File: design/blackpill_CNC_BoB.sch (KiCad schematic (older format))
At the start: 297 parts, among them J101 ALimIN, J102 ZLimIN, J103 YLimIN, J104 XLimIN, J105 CS_IN, J106 FH_IN, J107 DoorIN, J108 ResetIN, J109 ProbeIN, J110 12V Power in, J111 AuxEncIn, J112 5V Power out, J113 ADC_in_1, J114 ADC_in_2, J115 stepDriverLim, J116 Reset, J117 UART1, J118 I2C, J119 SpindleVFD, J120 Spindle/Coolant, J121 Spindle, J122 Coolant, J123 AuxOut, J124 XStepDrv, J125 YStepDrv, J126 ZStepDrv, J127 AStepDrv, U101 TLP290-4, U102 TLP290-4, U103 TLP290-4, U104 74LVC2G17, U105 LD1117S50TR_SOT223, U106 LM358, U107 TLV9001, U108 TLV9001, U109 YAAJ_WeAct_BlackPill_Part_Like, U110 TLV9001, U111 TLV9001, U112 74HCT541, U113 74HCT541, U114 74HCT541, U115 ULN2003A, U116 ULN2003A, U117 ULN2003A

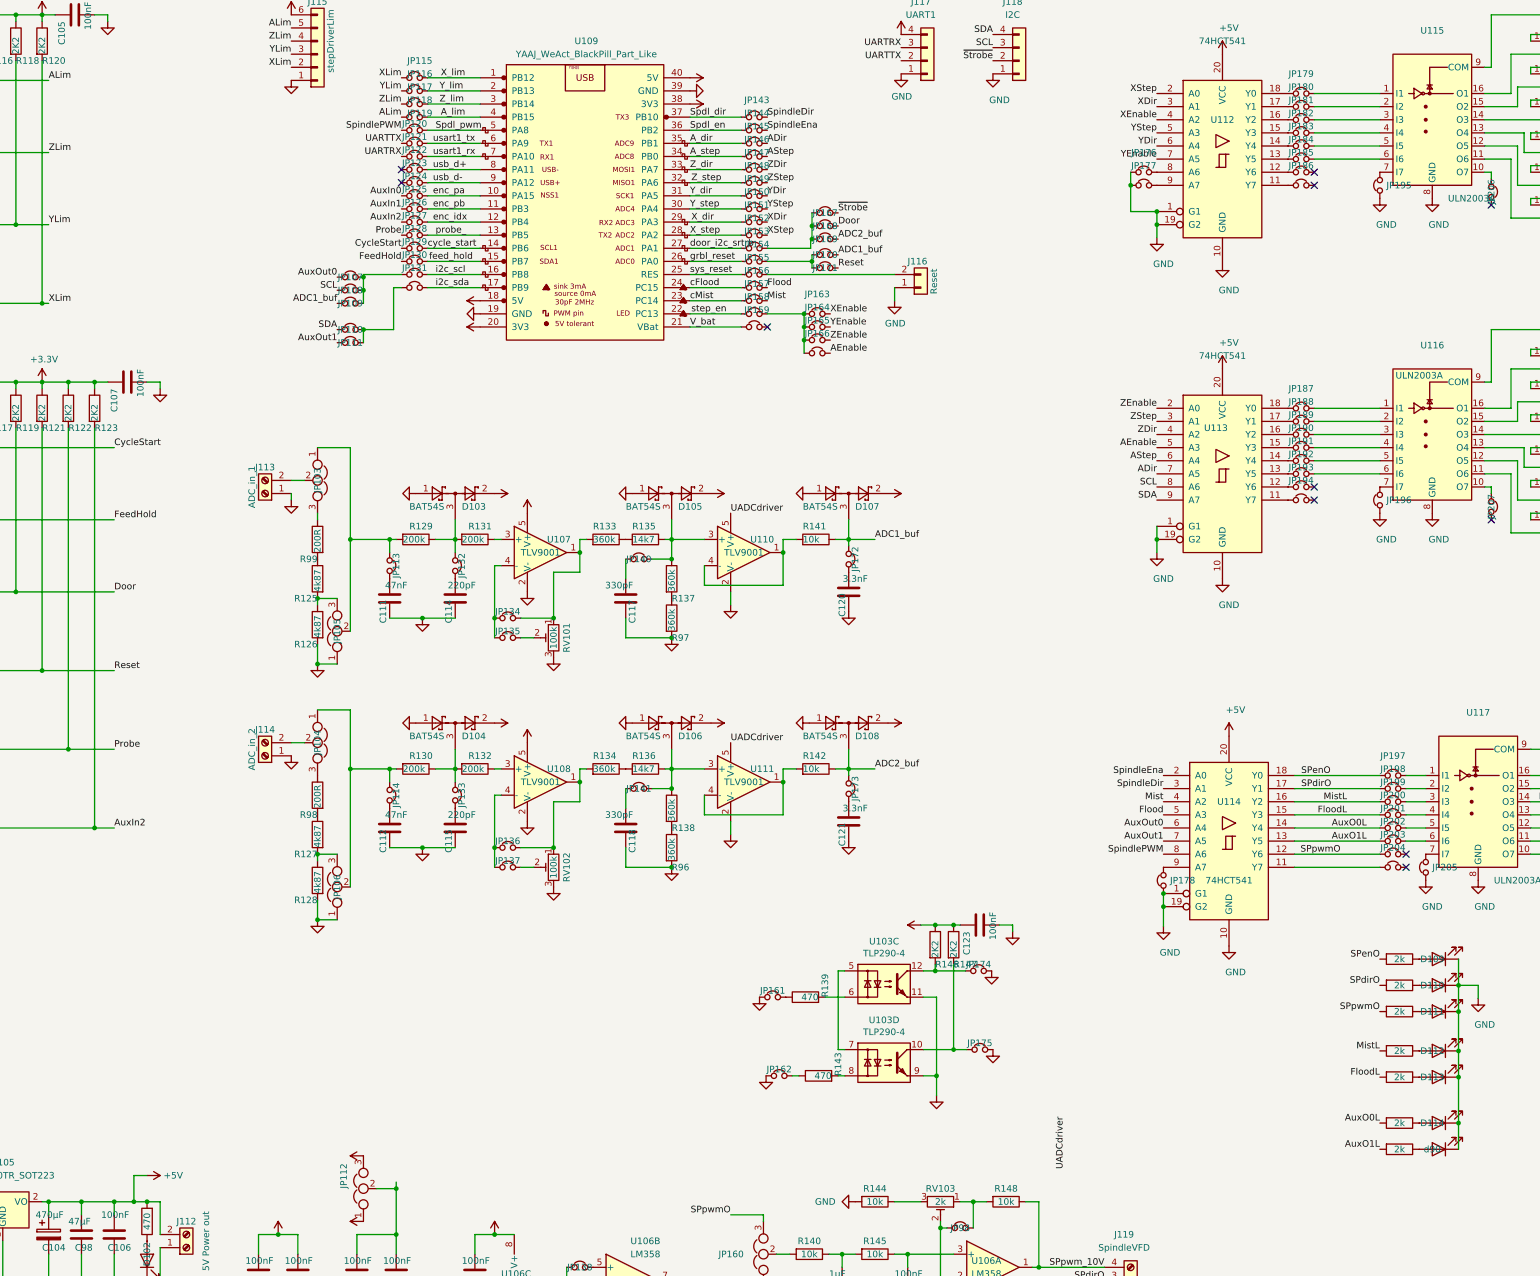
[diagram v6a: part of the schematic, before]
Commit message: add schottky to blackpill 5V
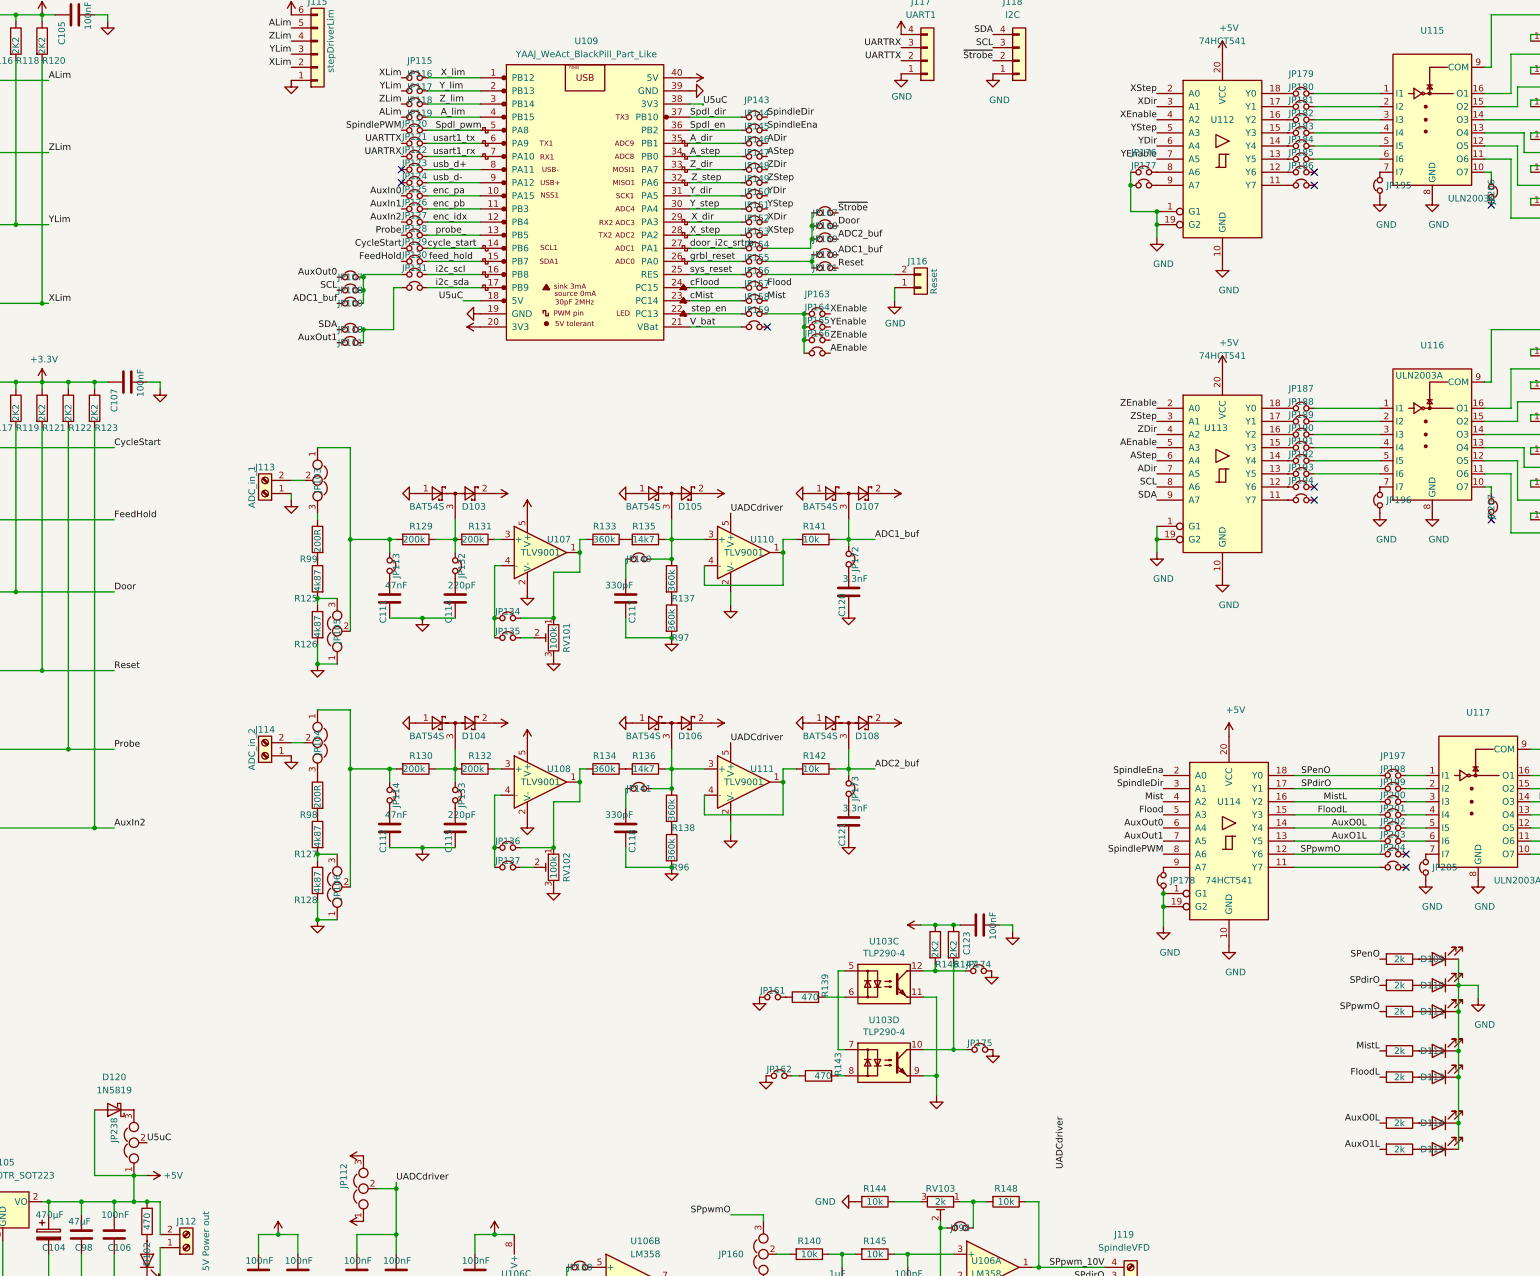
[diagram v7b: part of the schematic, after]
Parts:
- added D120: 1N5819, Diode_SMD:D_SOD-323, symbol Diode:1N5819
- added JP238: Jumper_NC_Dual, Connector_PinHeader_2.54mm:PinHeader_1x03_P2.54mm_Vertical, symbol Device:Jumper_NC_Dual
- renumbered d90 to D115, r90 to R167
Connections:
- net +5V: now also D120.2 (A), JP238.1; no longer U109.18 (5V), U109.38 (3V3)
- net UADCdriver: now also C110.1, C113.1, JP112.2
- new net: D120.1 (K), JP238.3
- new net U5uC: JP238.2, U109.18 (5V), U109.38 (3V3)
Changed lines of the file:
@@
 $EndComp
 $Comp
-L power:+5V #PWR0132
-U 1 1 6843DDDB
-P 6240 2980
-F 0 "#PWR0132" H 6240 2830 50  0001 C CNN
-F 1 "+5V" V 6260 3150 50  0001 L CNN
-F 2 "" H 6240 2980 50  0001 C CNN
-F 3 "" H 6240 2980 50  0001 C CNN
-	1    6240 2980
-	0    -1   -1   0
-$EndComp
-$Comp
 L power:GND #PWR0133
 U 1 1 6843E09C
@@
 	0    1    1    0
 $EndComp
-$Comp
-L power:+5V #PWR0152
-U 1 1 6860CDFC
-P 7840 1480
-F 0 "#PWR0152" H 7840 1330 50  0001 C CNN
-F 1 "+5V" V 7830 1620 50  0001 L CNN
-F 2 "" H 7840 1480 50  0001 C CNN
-F 3 "" H 7840 1480 50  0001 C CNN
-	1    7840 1480
-	0    1    1    0
-$EndComp
 NoConn ~ 8430 3180
 $Comp
@@
 Connection ~ 7700 7300
 $Comp
-L Device:R r90
+L Device:R R167
 U 1 1 67BECA90
 P 13250 9450
-F 0 "r90" V 13000 9450 50  0001 C CNN
+F 0 "R167" V 13000 9450 50  0001 C CNN
 F 1 "2k" V 13250 9450 50  0000 C CNN
 F 2 "Resistor_SMD:R_0603_1608Metric" V 13180 9450 50  0001 C CNN
@@
 $EndComp
 $Comp
-L Device:LED d90
+L Device:LED D115
 U 1 1 67BED2C6
 P 13550 9450
-F 0 "d90" H 13600 9450 50  0000 C CNN
+F 0 "D115" H 13600 9450 50  0000 C CNN
 F 1 "LED" H 13500 9250 50  0001 C CNN
 F 2 "LED_SMD:LED_0603_1608Metric" H 13550 9450 50  0001 C CNN
@@
 Wire Wire Line
 	2900 10850 3050 10850
+Text Label 5600 9700 0    50   ~ 0
+UADCdriver
+$Comp
+L Diode:1N5819 D120
+U 1 1 681EDD27
+P 3450 9150
+F 0 "D120" H 3450 8900 50  0000 C CNN
+F 1 "1N5819" H 3450 9000 50  0000 C CNN
+F 2 "Diode_SMD:D_SOD-323" H 3450 8975 50  0001 C CNN
+F 3 "http://www.vishay.com/docs/88525/1n5817.pdf" H 3450 9150 50  0001 C CNN
+	1    3450 9150
+	-1   0    0    1
+$EndComp
+$Comp
+L Device:Jumper_NC_Dual JP238
+U 1 1 681F0126
+P 3600 9400
+F 0 "JP238" H 3600 9550 50  0000 L CNN
+F 1 "Jumper_NC_Dual" V 3600 9550 50  0001 L CNN
+F 2 "Connector_PinHeader_2.54mm:PinHeader_1x03_P2.54mm_Vertical" H 3600 9400 50  0001 C CNN
+F 3 "~" H 3600 9400 50  0001 C CNN
+	1    3600 9400
+	0    -1   -1   0
+$EndComp
+Connection ~ 3600 9650
+Wire Wire Line
+	3600 9650 3300 9650
+Wire Wire Line
+	3300 9650 3300 9150
+Text Label 3700 9400 0    50   ~ 0
+U5uC
+Text Label 7940 1490 0    50   ~ 0
+U5uC
+Text Label 6110 2980 2    50   ~ 0
+U5uC
+Wire Wire Line
+	7840 1480 7940 1480
+Wire Wire Line
+	7940 1480 7940 1490
+Wire Wire Line
+	6240 2980 6110 2980
 $EndSCHEMATC

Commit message: change screw terminals and start placing analog in
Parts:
- J101, J102, J103, J104, J105, J106, J107, J108, J109, J113, J114: footprint Connector_Phoenix_MSTB:PhoenixContact_MSTBA_2,5_2-G-5,08_1x02_P5.08mm_Horizontal -> conn_my_kf128:ScrewTerminal_1x2_P2.54mm_Vertical
- J119, J121, J122, J123, J124, J125, J126, J127: footprint Connector_Phoenix_MSTB:PhoenixContact_MSTBA_2,5_4-G-5,08_1x04_P5.08mm_Horizontal -> conn_my_kf128:ScrewTerminal_1x4_P2.54mm_Vertical
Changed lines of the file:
@@
 F 0 "J124" H 15750 1000 50  0000 L CNN
 F 1 "XStepDrv" H 15750 900 50  0000 L CNN
-F 2 "Connector_Phoenix_MSTB:PhoenixContact_MSTBA_2,5_4-G-5,08_1x04_P5.08mm_Horizontal" H 15650 1000 50  0001 C CNN
+F 2 "conn_my_kf128:ScrewTerminal_1x4_P2.54mm_Vertical" H 15650 1000 50  0001 C CNN
 F 3 "~" H 15650 1000 50  0001 C CNN
 	1    15650 1000
@@
 F 0 "J125" H 15750 2150 50  0000 L CNN
 F 1 "YStepDrv" H 15750 2050 50  0000 L CNN
-F 2 "Connector_Phoenix_MSTB:PhoenixContact_MSTBA_2,5_4-G-5,08_1x04_P5.08mm_Horizontal" H 15650 2150 50  0001 C CNN
+F 2 "conn_my_kf128:ScrewTerminal_1x4_P2.54mm_Vertical" H 15650 2150 50  0001 C CNN
 F 3 "~" H 15650 2150 50  0001 C CNN
 	1    15650 2150
@@
 F 0 "J126" H 15750 3400 50  0000 L CNN
 F 1 "ZStepDrv" H 15750 3300 50  0000 L CNN
-F 2 "Connector_Phoenix_MSTB:PhoenixContact_MSTBA_2,5_4-G-5,08_1x04_P5.08mm_Horizontal" H 15650 3400 50  0001 C CNN
+F 2 "conn_my_kf128:ScrewTerminal_1x4_P2.54mm_Vertical" H 15650 3400 50  0001 C CNN
 F 3 "~" H 15650 3400 50  0001 C CNN
 	1    15650 3400
@@
 F 0 "J127" H 15750 4550 50  0000 L CNN
 F 1 "AStepDrv" H 15750 4450 50  0000 L CNN
-F 2 "Connector_Phoenix_MSTB:PhoenixContact_MSTBA_2,5_4-G-5,08_1x04_P5.08mm_Horizontal" H 15650 4550 50  0001 C CNN
+F 2 "conn_my_kf128:ScrewTerminal_1x4_P2.54mm_Vertical" H 15650 4550 50  0001 C CNN
 F 3 "~" H 15650 4550 50  0001 C CNN
 	1    15650 4550
@@
 F 0 "J121" H 15400 8000 50  0000 L CNN
 F 1 "Spindle" H 15400 7900 50  0000 L CNN
-F 2 "Connector_Phoenix_MSTB:PhoenixContact_MSTBA_2,5_4-G-5,08_1x04_P5.08mm_Horizontal" H 15300 8000 50  0001 C CNN
+F 2 "conn_my_kf128:ScrewTerminal_1x4_P2.54mm_Vertical" H 15300 8000 50  0001 C CNN
 F 3 "~" H 15300 8000 50  0001 C CNN
 	1    15300 8000
@@
 F 0 "J122" H 15400 8700 50  0000 L CNN
 F 1 "Coolant" H 15400 8600 50  0000 L CNN
-F 2 "Connector_Phoenix_MSTB:PhoenixContact_MSTBA_2,5_4-G-5,08_1x04_P5.08mm_Horizontal" H 15300 8700 50  0001 C CNN
+F 2 "conn_my_kf128:ScrewTerminal_1x4_P2.54mm_Vertical" H 15300 8700 50  0001 C CNN
 F 3 "~" H 15300 8700 50  0001 C CNN
 	1    15300 8700
@@
 F 0 "J123" H 15400 9250 50  0000 L CNN
 F 1 "AuxOut" H 15400 9150 50  0000 L CNN
-F 2 "Connector_Phoenix_MSTB:PhoenixContact_MSTBA_2,5_4-G-5,08_1x04_P5.08mm_Horizontal" H 15300 9250 50  0001 C CNN
+F 2 "conn_my_kf128:ScrewTerminal_1x4_P2.54mm_Vertical" H 15300 9250 50  0001 C CNN
 F 3 "~" H 15300 9250 50  0001 C CNN
 	1    15300 9250
@@
 F 0 "J119" H 11150 10100 50  0000 C CNN
 F 1 "SpindleVFD" H 11150 10200 50  0000 C CNN
-F 2 "Connector_Phoenix_MSTB:PhoenixContact_MSTBA_2,5_4-G-5,08_1x04_P5.08mm_Horizontal" H 11200 10550 50  0001 C CNN
+F 2 "conn_my_kf128:ScrewTerminal_1x4_P2.54mm_Vertical" H 11200 10550 50  0001 C CNN
 F 3 "~" H 11200 10550 50  0001 C CNN
 	1    11200 10550
@@
 F 0 "J101" H 750 1400 50  0000 C CNN
 F 1 "ALimIN" V 850 1550 50  0000 C CNN
-F 2 "Connector_Phoenix_MSTB:PhoenixContact_MSTBA_2,5_2-G-5,08_1x02_P5.08mm_Horizontal" H 750 1600 50  0001 C CNN
+F 2 "conn_my_kf128:ScrewTerminal_1x2_P2.54mm_Vertical" H 750 1600 50  0001 C CNN
 F 3 "~" H 750 1600 50  0001 C CNN
 	1    750  1600
@@
 F 0 "J102" H 750 1950 50  0000 C CNN
 F 1 "ZLimIN" V 850 2100 50  0000 C CNN
-F 2 "Connector_Phoenix_MSTB:PhoenixContact_MSTBA_2,5_2-G-5,08_1x02_P5.08mm_Horizontal" H 750 2150 50  0001 C CNN
+F 2 "conn_my_kf128:ScrewTerminal_1x2_P2.54mm_Vertical" H 750 2150 50  0001 C CNN
 F 3 "~" H 750 2150 50  0001 C CNN
 	1    750  2150
@@
 F 0 "J103" H 750 2500 50  0000 C CNN
 F 1 "YLimIN" V 850 2650 50  0000 C CNN
-F 2 "Connector_Phoenix_MSTB:PhoenixContact_MSTBA_2,5_2-G-5,08_1x02_P5.08mm_Horizontal" H 750 2700 50  0001 C CNN
+F 2 "conn_my_kf128:ScrewTerminal_1x2_P2.54mm_Vertical" H 750 2700 50  0001 C CNN
 F 3 "~" H 750 2700 50  0001 C CNN
 	1    750  2700
@@
 F 0 "J104" H 750 3100 50  0000 C CNN
 F 1 "XLimIN" V 850 3250 50  0000 C CNN
-F 2 "Connector_Phoenix_MSTB:PhoenixContact_MSTBA_2,5_2-G-5,08_1x02_P5.08mm_Horizontal" H 750 3300 50  0001 C CNN
+F 2 "conn_my_kf128:ScrewTerminal_1x2_P2.54mm_Vertical" H 750 3300 50  0001 C CNN
 F 3 "~" H 750 3300 50  0001 C CNN
 	1    750  3300
@@
 F 0 "J105" H 750 4200 50  0000 C CNN
 F 1 "CS_IN" V 850 4350 50  0000 C CNN
-F 2 "Connector_Phoenix_MSTB:PhoenixContact_MSTBA_2,5_2-G-5,08_1x02_P5.08mm_Horizontal" H 750 4400 50  0001 C CNN
+F 2 "conn_my_kf128:ScrewTerminal_1x2_P2.54mm_Vertical" H 750 4400 50  0001 C CNN
 F 3 "~" H 750 4400 50  0001 C CNN
 	1    750  4400
@@
 F 0 "J106" H 750 4750 50  0000 C CNN
 F 1 "FH_IN" V 850 4900 50  0000 C CNN
-F 2 "Connector_Phoenix_MSTB:PhoenixContact_MSTBA_2,5_2-G-5,08_1x02_P5.08mm_Horizontal" H 750 4950 50  0001 C CNN
+F 2 "conn_my_kf128:ScrewTerminal_1x2_P2.54mm_Vertical" H 750 4950 50  0001 C CNN
 F 3 "~" H 750 4950 50  0001 C CNN
 	1    750  4950
@@
 F 0 "J107" H 750 5300 50  0000 C CNN
 F 1 "DoorIN" V 850 5450 50  0000 C CNN
-F 2 "Connector_Phoenix_MSTB:PhoenixContact_MSTBA_2,5_2-G-5,08_1x02_P5.08mm_Horizontal" H 750 5500 50  0001 C CNN
+F 2 "conn_my_kf128:ScrewTerminal_1x2_P2.54mm_Vertical" H 750 5500 50  0001 C CNN
 F 3 "~" H 750 5500 50  0001 C CNN
 	1    750  5500
@@
 F 0 "J108" H 750 5900 50  0000 C CNN
 F 1 "ResetIN" V 850 6050 50  0000 C CNN
-F 2 "Connector_Phoenix_MSTB:PhoenixContact_MSTBA_2,5_2-G-5,08_1x02_P5.08mm_Horizontal" H 750 6100 50  0001 C CNN
+F 2 "conn_my_kf128:ScrewTerminal_1x2_P2.54mm_Vertical" H 750 6100 50  0001 C CNN
 F 3 "~" H 750 6100 50  0001 C CNN
 	1    750  6100
@@
 F 0 "J109" H 750 6500 50  0000 C CNN
 F 1 "ProbeIN" V 850 6650 50  0000 C CNN
-F 2 "Connector_Phoenix_MSTB:PhoenixContact_MSTBA_2,5_2-G-5,08_1x02_P5.08mm_Horizontal" H 750 6700 50  0001 C CNN
+F 2 "conn_my_kf128:ScrewTerminal_1x2_P2.54mm_Vertical" H 750 6700 50  0001 C CNN
 F 3 "~" H 750 6700 50  0001 C CNN
 	1    750  6700
@@
 F 0 "J113" H 4600 4250 50  0000 C CNN
 F 1 "ADC_in_1" V 4700 4400 50  0000 C CNN
-F 2 "Connector_Phoenix_MSTB:PhoenixContact_MSTBA_2,5_2-G-5,08_1x02_P5.08mm_Horizontal" H 4600 4450 50  0001 C CNN
+F 2 "conn_my_kf128:ScrewTerminal_1x2_P2.54mm_Vertical" H 4600 4450 50  0001 C CNN
 F 3 "~" H 4600 4450 50  0001 C CNN
 	1    4600 4450
@@
 F 0 "J114" H 4600 6250 50  0000 C CNN
 F 1 "ADC_in_2" V 4700 6400 50  0000 C CNN
-F 2 "Connector_Phoenix_MSTB:PhoenixContact_MSTBA_2,5_2-G-5,08_1x02_P5.08mm_Horizontal" H 4600 6450 50  0001 C CNN
+F 2 "conn_my_kf128:ScrewTerminal_1x2_P2.54mm_Vertical" H 4600 6450 50  0001 C CNN
 F 3 "~" H 4600 6450 50  0001 C CNN
 	1    4600 6450
